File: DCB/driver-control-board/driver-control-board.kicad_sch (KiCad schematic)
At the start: 32 parts, among them J1 Conn_01x05, J2 Conn_01x14, J3 Conn_01x08, J4 Conn_01x23, J5 Conn_02x10_Counter_Clockwise, J6 Conn_01x14, U1 STM32F413CGUx, U2 LD1117S33TR_SOT223, U3 R-78B5.0-2.0, U4 MCP2551-I-SN, Y1 Crystal

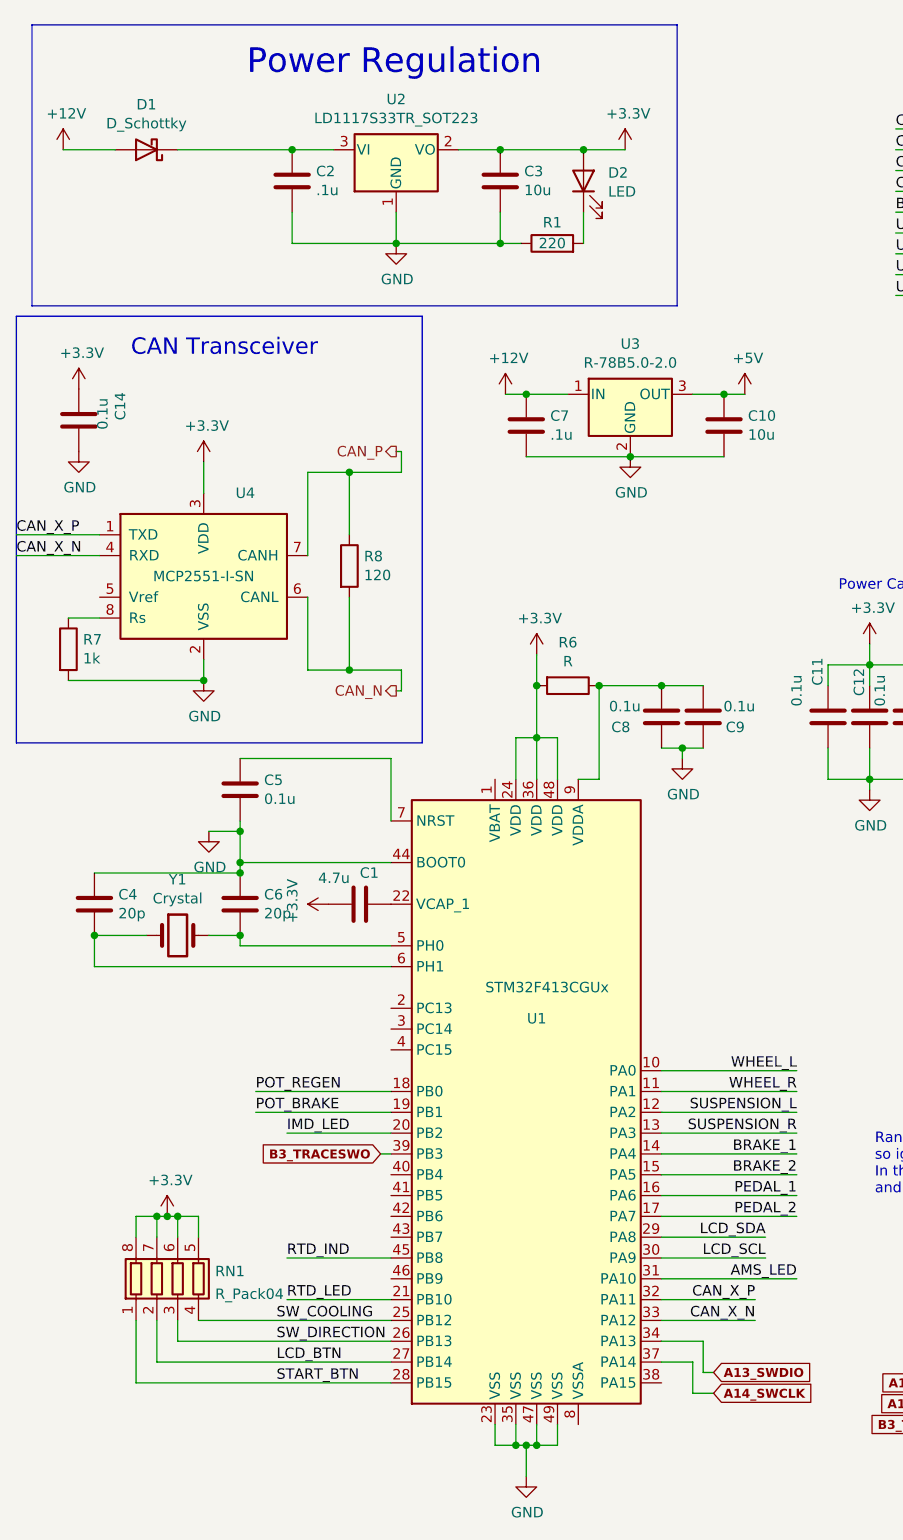
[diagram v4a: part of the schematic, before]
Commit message: Major Review and Part Update
updating footprints, component values, layouts
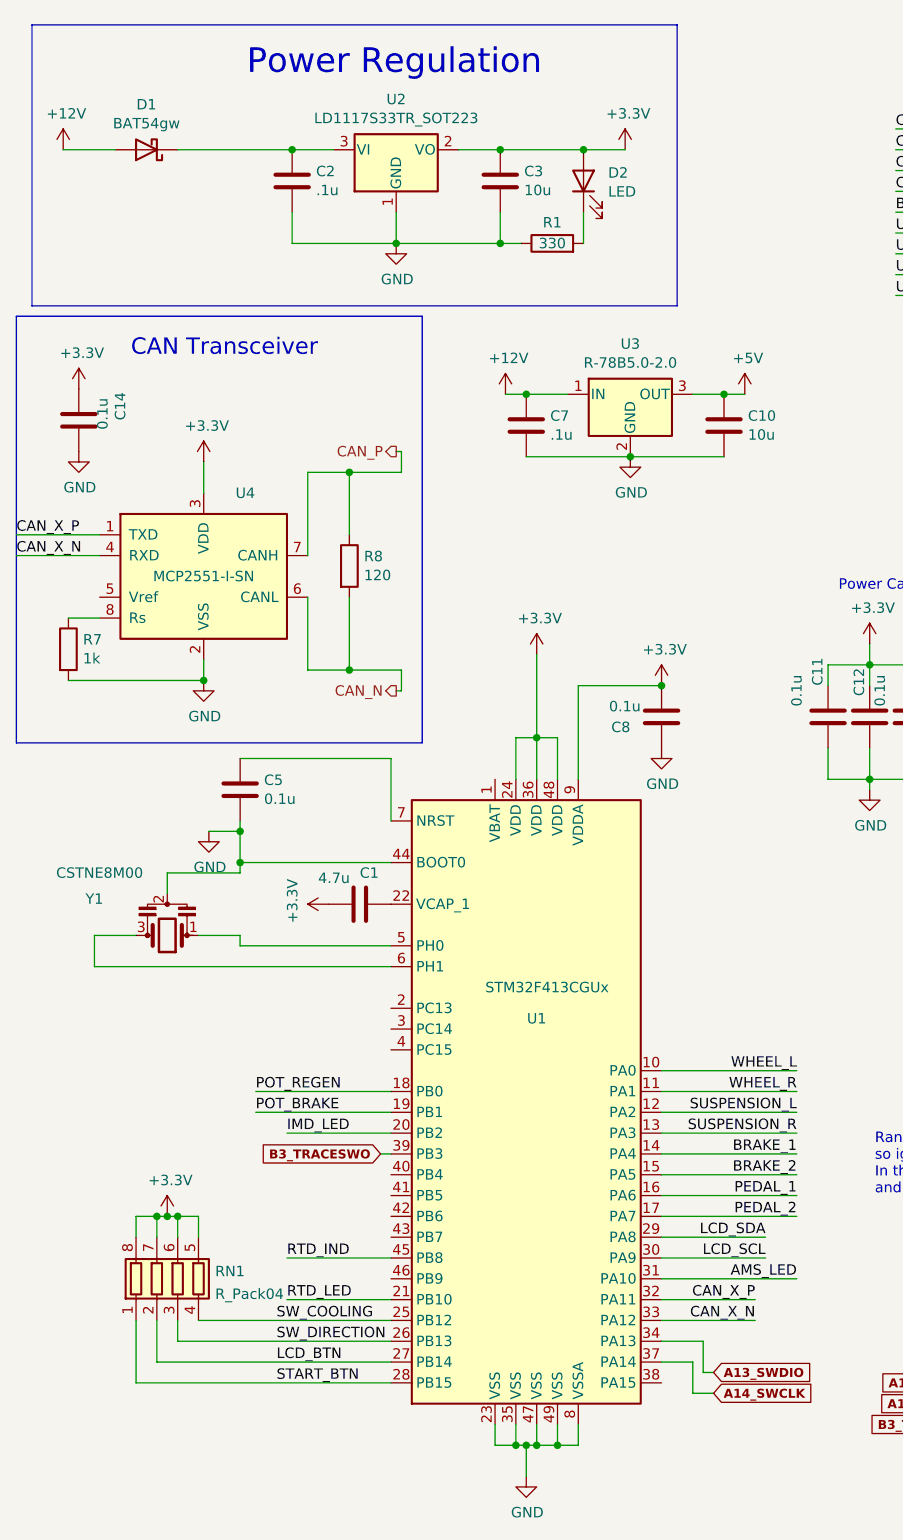
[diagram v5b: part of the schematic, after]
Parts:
- removed C4, C6: 20p, Capacitor_SMD:C_0603_1608Metric_Pad1.08x0.95mm_HandSolder, symbol Device:C
- removed C9: 0.1u, Capacitor_SMD:C_0603_1608Metric_Pad1.08x0.95mm_HandSolder, symbol Device:C
- removed R6: R, Resistor_SMD:R_0603_1608Metric_Pad0.98x0.95mm_HandSolder, symbol Device:R
- removed Y1: Crystal, Crystal:Crystal_HC52-8mm_Vertical, symbol Device:Crystal
- added Y1: CSTNE8M00, AERO_Footprints:Resonator_SMD_muRata_CSTxExxV-3Pin_3.0x1.1mm_HandSoldering, symbol Device:Resonator
- D1: value D_Schottky -> BAT54gw; footprint Diode_SMD:D_SMA-SMB_Universal_Handsoldering -> Diode_SMD:D_SOD-123
- R1: value 220 -> 330
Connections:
- net +3V3: now also C8.2, U1.9 (VDDA)
- net GND: now also U1.8 (VSSA), Y1.2
- net at U1.5 (PH0): now also Y1.1
- net at U1.6 (PH1): now also Y1.3

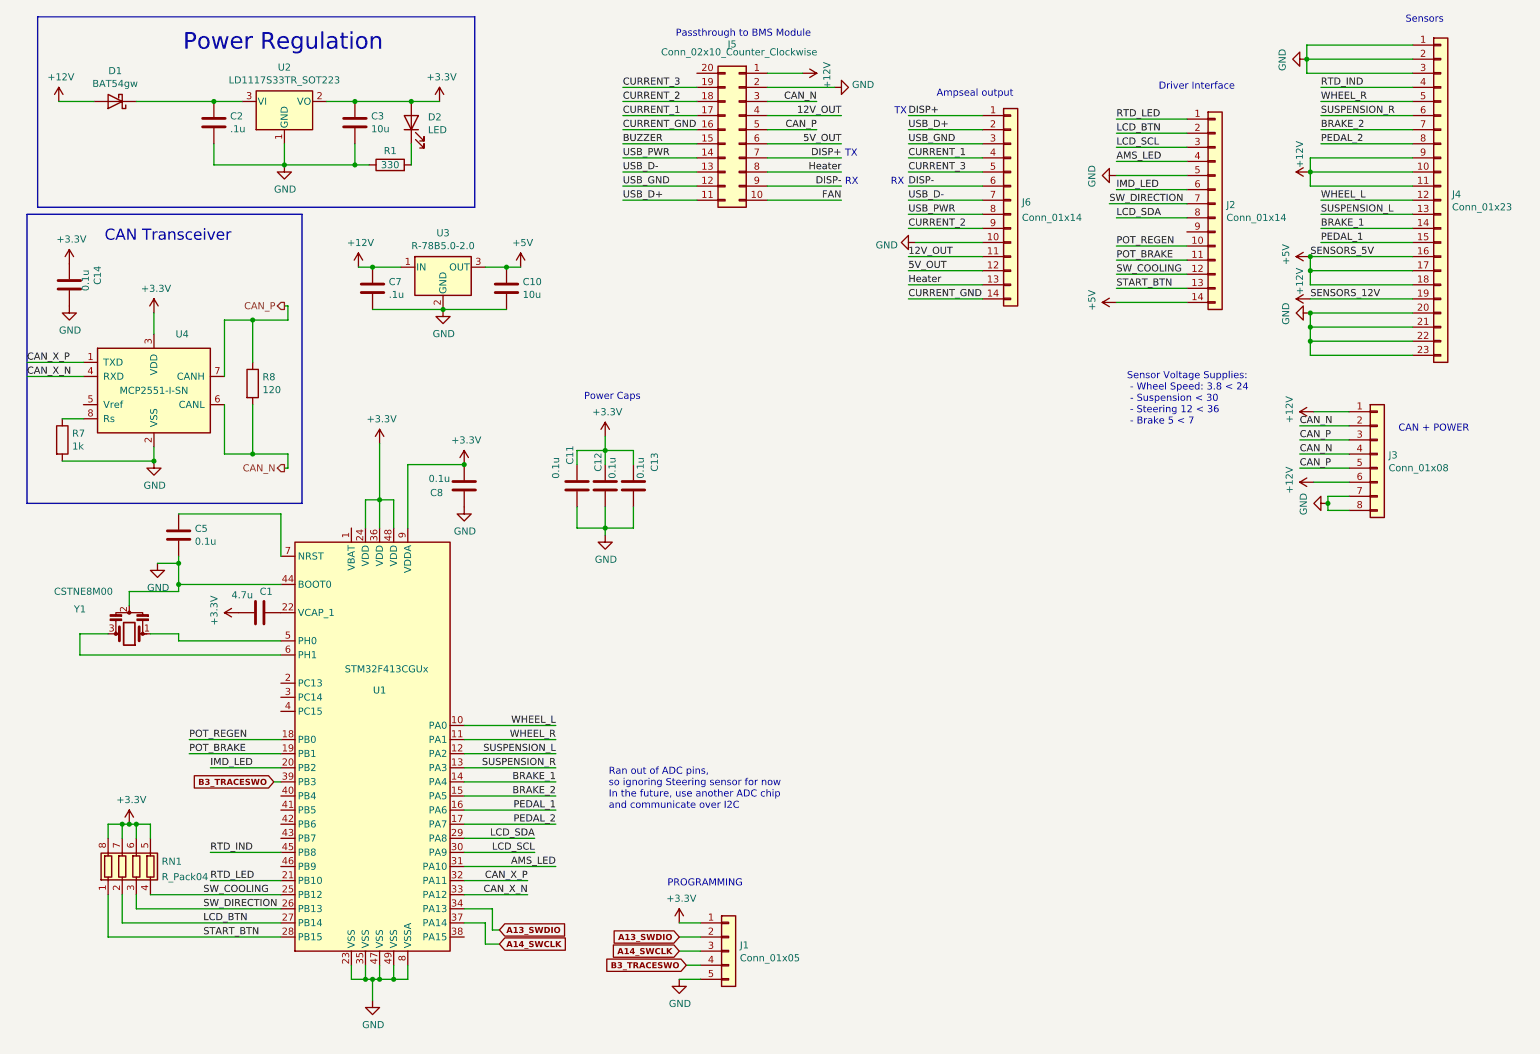
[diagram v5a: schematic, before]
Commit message: updating schematic based on RCB changes
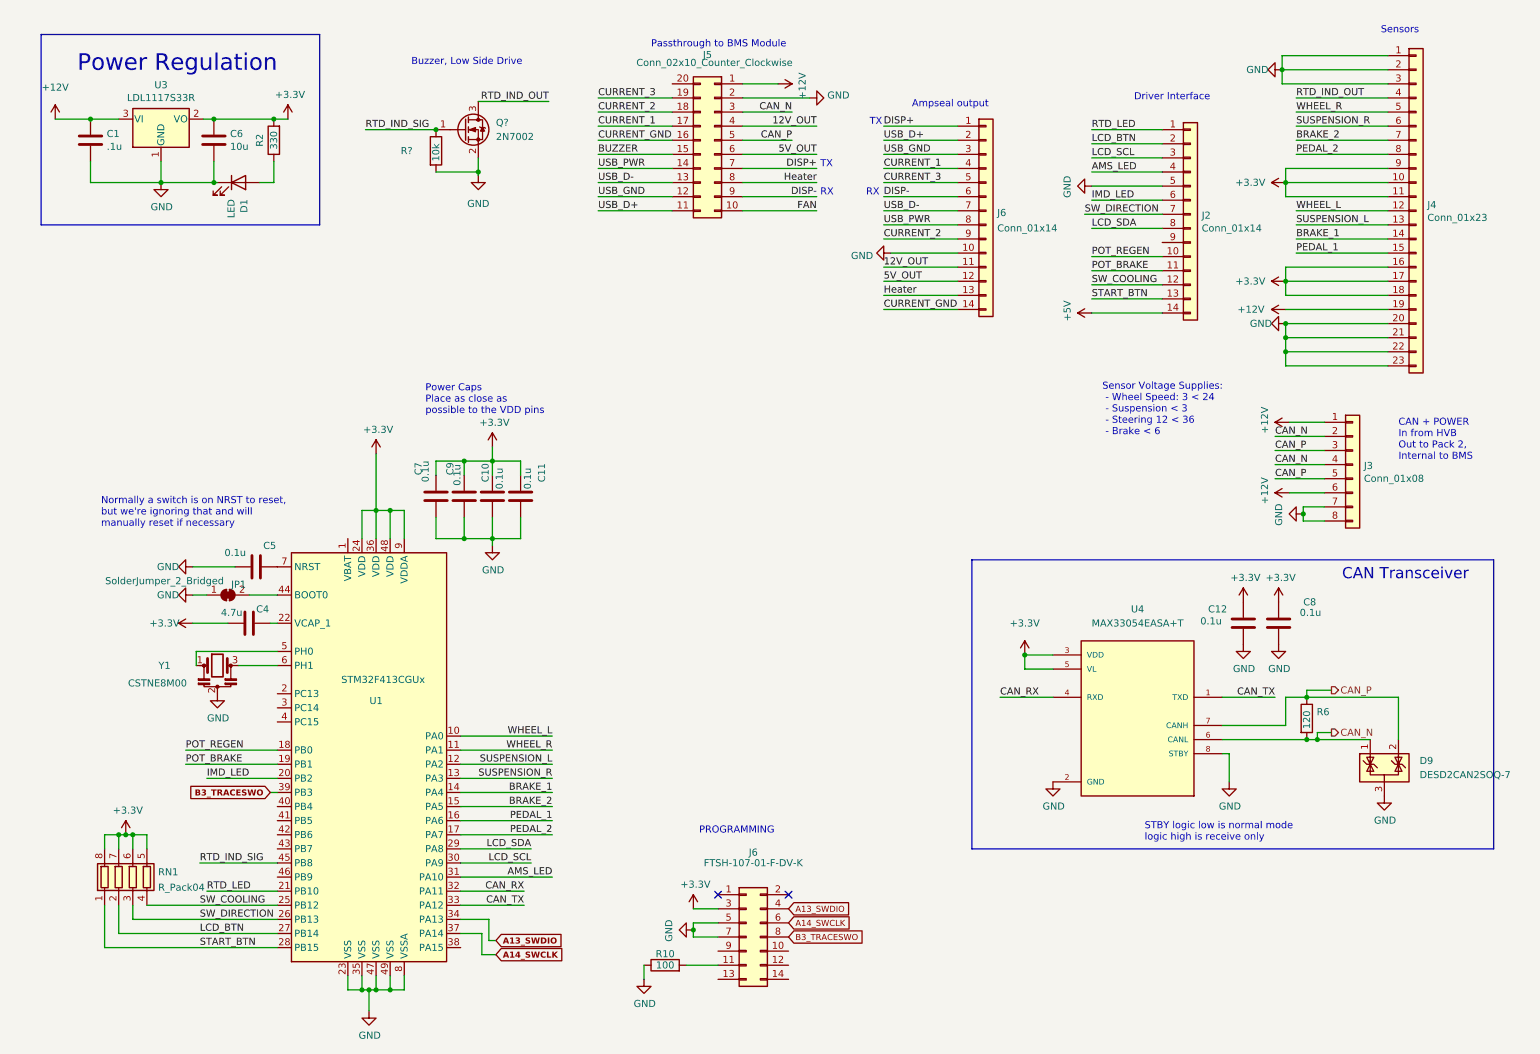
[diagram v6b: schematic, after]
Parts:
- removed C13, C14: 0.1u, Capacitor_SMD:C_0603_1608Metric_Pad1.08x0.95mm_HandSolder, symbol Device:C
- removed C2: .1u, Capacitor_SMD:C_0603_1608Metric_Pad1.08x0.95mm_HandSolder, symbol Device:C
- removed C3: 10u, Capacitor_SMD:C_0603_1608Metric_Pad1.08x0.95mm_HandSolder, symbol Device:C
- removed D1: BAT54gw, Diode_SMD:D_SOD-123, symbol Device:D_Schottky
- removed D2: LED, LED_SMD:LED_0603_1608Metric_Pad1.05x0.95mm_HandSolder, symbol Device:LED
- removed J1: Conn_01x05, Connector_JST:JST_XH_B5B-XH-A_1x05_P2.50mm_Vertical, symbol Connector_Generic:Conn_01x05
- removed R1: 330, Resistor_SMD:R_0603_1608Metric_Pad0.98x0.95mm_HandSolder, symbol Device:R
- removed R7: 1k, Resistor_SMD:R_0603_1608Metric_Pad0.98x0.95mm_HandSolder, symbol Device:R
- removed R8: 120, Resistor_SMD:R_0603_1608Metric_Pad0.98x0.95mm_HandSolder, symbol Device:R
- removed U2: LD1117S33TR_SOT223, Package_TO_SOT_SMD:SOT-223-3_TabPin2, symbol Regulator_Linear:LD1117S33TR_SOT223
- removed U3: R-78B5.0-2.0, Converter_DCDC:Converter_DCDC_RECOM_R-78B-2.0_THT, symbol Regulator_Switching:R-78B5.0-2.0
- removed U4: MCP2551-I-SN, Package_SO:SOIC-8_3.9x4.9mm_P1.27mm, symbol Interface_CAN_LIN:MCP2551-I-SN
- added C4: 4.7u, Capacitor_SMD:C_0603_1608Metric_Pad1.08x0.95mm_HandSolder, symbol Device:C
- added C6: 10u, Capacitor_SMD:C_0603_1608Metric_Pad1.08x0.95mm_HandSolder, symbol Device:C
- added C9: 0.1u, Capacitor_SMD:C_0603_1608Metric_Pad1.08x0.95mm_HandSolder, symbol Device:C
- added D1: LED, LED_SMD:LED_0603_1608Metric_Pad1.05x0.95mm_HandSolder, symbol Device:LED
- added D9: DESD2CAN2SOQ-7, Package_TO_SOT_SMD:SOT-23, symbol Power_Protection:NUP2105L
- added J6: FTSH-107-01-F-DV-K, Connector_PinHeader_1.27mm:PinHeader_2x07_P1.27mm_Vertical_SMD, symbol Connector_Generic:Conn_02x07_Odd_Even
- added JP1: SolderJumper_2_Bridged, Jumper:SolderJumper-2_P1.3mm_Bridged_Pad1.0x1.5mm, symbol Jumper:SolderJumper_2_Bridged
- added Q?: 2N7002, Package_TO_SOT_SMD:SOT-23, symbol Transistor_FET:2N7002
- added R10: 100, Resistor_SMD:R_0603_1608Metric_Pad0.98x0.95mm_HandSolder, symbol Device:R
- added R2: 330, Resistor_SMD:R_0603_1608Metric_Pad0.98x0.95mm_HandSolder, symbol Device:R
- added R6: 120, Resistor_SMD:R_0603_1608Metric_Pad0.98x0.95mm_HandSolder, symbol Device:R
- added R?: 10k, symbol Device:R
- added U3: LDL1117S33R, Package_TO_SOT_SMD:SOT-223-3_TabPin2, symbol Regulator_Linear:LD1117S33TR_SOT223
- added U4: MAX33054EASA+T, AERO_Footprints:SOIC127P600X175-8N, symbol AERO_Symbols:MAX33054EASA+T
- C1: value 4.7u -> .1u
- C10: value 10u -> 0.1u
- C7: value .1u -> 0.1u
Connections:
- net +12V: now also C1.1, U3.3 (VI); no longer C7.1, J4.10 (Pin_10), J4.11 (Pin_11), J4.9 (Pin_9)
- net +3V3: now also C10.1, C7.1, C8.1, J4.10 (Pin_10), J4.11 (Pin_11), J4.16 (Pin_16), J4.17 (Pin_17), J4.18 (Pin_18), J4.9 (Pin_9), C4.2, C6.1, C9.1, J6.3 (Pin_3), R2.2, U3.2 (VO), U4.3 (VDD), U4.5 (VL); no longer C1.2, C8.2
- net +5V: no longer C10.1, J4.16 (Pin_16), J4.17 (Pin_17), J4.18 (Pin_18)
- net A13_SWDIO: now also J6.4 (Pin_4)
- net A14_SWCLK: now also J6.6 (Pin_6)
- net B3_TRACESWO: now also J6.8 (Pin_8)
- net CAN_N: now also D9.1 (K), R6.2, U4.6 (CANL)
- net CAN_P: now also D9.2 (K), R6.1, U4.7 (CANH)
- net GND: now also C1.2, C8.2, C6.2, C9.2, D1.1 (K), D9.3 (A), J6.5 (Pin_5), J6.7 (Pin_7), JP1.1 (A), Q?.2 (S), R10.1, R?.2, U3.1 (GND), U4.2 (GND), U4.8 (STBY); no longer C8.1, U1.44 (BOOT0)
- net at U1.22 (VCAP_1): now also C4.1; no longer C1.1
- net CAN_X_N renamed CAN_TX
- net CAN_TX: now also U4.1 (TXD)
- net CAN_X_P renamed CAN_RX
- net CAN_RX: now also U4.4 (RXD)
- net RTD_IND renamed RTD_IND_OUT
- net RTD_IND_OUT: now also Q?.3 (D); no longer U1.45 (PB8)
- new net: J6.11 (Pin_11), R10.2
- new net: JP1.2 (B), U1.44 (BOOT0)
- new net: D1.2 (A), R2.1
- new net RTD_IND_SIG: Q?.1 (G), R?.1, U1.45 (PB8)
- no-connect marks 0 -> 2
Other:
- note added: "Buzzer, Low Side Drive"
- note added: "CAN + POWER In from HVB Out to Pack 2, Internal to BMS"
- note added: "Normally a switch is on NRST to reset, but we're ignoring that and will manually reset if necessary"
- note added: "Power Caps Place as close as possible to the VDD pins"
- note added: "STBY logic low is normal mode logic high is receive only"
- note added: "Sensor Voltage Supplies: - Wheel Speed: 3 < 24 - Suspension < 3 - Steering 12 < 36 - Brake < 6"
- note removed: "CAN + POWER"
- note removed: "Power Caps"
- note removed: "Ran out of ADC pins, so ignoring Steering sensor for now In the future, use another ADC chip and communicate over I2C"
- note removed: "Sensor Voltage Supplies: - Wheel Speed: 3.8 < 24 - Suspension < 30 - Steering 12 < 36 - Brake 5 < 7"
- moved on the sheet: J2, J3, J4, J5, J6, RN1

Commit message: updating schem and layout. WIP
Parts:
- added D2, D3, D4, D5, D6: SP0502BAHT, Package_TO_SOT_SMD:SOT-23, symbol Power_Protection:SP0502BAHT
- R1: renamed from R?; footprint (none) -> Resistor_SMD:R_0603_1608Metric_Pad0.98x0.95mm_HandSolder
- gave numbers to parts that had none: 1
- renumbered J6 to J7
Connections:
- net BRAKE_1: now also D4.2 (K)
- net BRAKE_2: now also D4.1 (K)
- net GND: now also D2.3 (A), D3.3 (A), D4.3 (A), D5.3 (A), D6.3 (A)
- net PEDAL_1: now also D3.2 (K)
- net PEDAL_2: now also D3.1 (K)
- net POT_BRAKE: now also D2.2 (K)
- net POT_REGEN: now also D2.1 (K)
- net SUSPENSION_L: now also D5.2 (K)
- net SUSPENSION_R: now also D5.1 (K)
- net WHEEL_L: now also D6.2 (K)
- net WHEEL_R: now also D6.1 (K)
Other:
- moved on the sheet: J7, R10

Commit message: finished schem and layout. Ready for Review
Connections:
- net +5V is gone; now on net +3V3: J2.14 (Pin_14)
- net +12V: now also J4.16 (Pin_16); no longer J4.19 (Pin_19)
- net +3V3: no longer J4.16 (Pin_16)
- net GND: no longer J4.1 (Pin_1)
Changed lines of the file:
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@@
-    (stroke (width 0) (type default) (color 0 0 0 0))
-  )
-  (wire (pts (xy 242.57 59.055) (xy 242.57 61.595))
     (stroke (width 0) (type default) (color 0 0 0 0))
   )
@@
   )
   (wire (pts (xy 158.115 43.815) (xy 144.78 43.815))
-    (stroke (width 0) (type default) (color 0 0 0 0))
-  )
-  (wire (pts (xy 241.935 23.495) (xy 241.935 20.955))
     (stroke (width 0) (type default) (color 0 0 0 0))
   )
@@
     (pin "1")
   )
-  (symbol (lib_id "power:+5V") (at 207.645 67.31 90) (unit 1)
-    (in_bom yes) (on_board yes)
-    (property "Reference" "#PWR0115" (id 0) (at 211.455 67.31 0)
-      (effects (font (size 1.27 1.27)) hide)
-    )
-    (property "Value" "+5V" (id 1) (at 203.2508 66.929 0))
-    (property "Footprint" "" (id 2) (at 207.645 67.31 0)
-      (effects (font (size 1.27 1.27)) hide)
-    )
-    (property "Datasheet" "" (id 3) (at 207.645 67.31 0)
-      (effects (font (size 1.27 1.27)) hide)
-    )
-    (pin "1")
-  )
   (symbol (lib_id "power:GND") (at 207.645 44.45 270) (unit 1)
     (in_bom yes) (on_board yes)
@@
     (pin "8")
   )
-  (symbol (lib_id "power:+12V") (at 242.57 66.675 90) (unit 1)
+  (symbol (lib_id "power:+12V") (at 242.57 59.055 90) (unit 1)
     (in_bom yes) (on_board yes) (fields_autoplaced)
-    (property "Reference" "#PWR0101" (id 0) (at 246.38 66.675 0)
-      (effects (font (size 1.27 1.27)) hide)
-    )
-    (property "Value" "+12V" (id 1) (at 238.76 66.6749 90)
-      (effects (font (size 1.27 1.27)) (justify left))
-    )
-    (property "Footprint" "" (id 2) (at 242.57 66.675 0)
-      (effects (font (size 1.27 1.27)) hide)
-    )
-    (property "Datasheet" "" (id 3) (at 242.57 66.675 0)
+    (property "Reference" "#PWR0101" (id 0) (at 246.38 59.055 0)
+      (effects (font (size 1.27 1.27)) hide)
+    )
+    (property "Value" "+12V" (id 1) (at 238.76 59.0549 90)
+      (effects (font (size 1.27 1.27)) (justify left))
+    )
+    (property "Footprint" "" (id 2) (at 242.57 59.055 0)
+      (effects (font (size 1.27 1.27)) hide)
+    )
+    (property "Datasheet" "" (id 3) (at 242.57 59.055 0)
       (effects (font (size 1.27 1.27)) hide)
     )
@@
     (pin "3")
   )
+  (symbol (lib_id "power:+3.3V") (at 207.645 67.31 90) (unit 1)
+    (in_bom yes) (on_board yes)
+    (property "Reference" "#PWR0115" (id 0) (at 211.455 67.31 0)
+      (effects (font (size 1.27 1.27)) hide)
+    )
+    (property "Value" "+3.3V" (id 1) (at 201.295 67.31 90))
+    (property "Footprint" "" (id 2) (at 207.645 67.31 0)
+      (effects (font (size 1.27 1.27)) hide)
+    )
+    (property "Datasheet" "" (id 3) (at 207.645 67.31 0)
+      (effects (font (size 1.27 1.27)) hide)
+    )
+    (pin "1")
+  )
   (symbol (lib_id "power:GND") (at 241.935 23.495 270) (unit 1)
     (in_bom yes) (on_board yes)
@@
       (reference "#PWR0114") (unit 1) (value "+3.3V") (footprint "")
     )
-    (path "/00000000-0000-0000-0000-000061fdabd7"
-      (reference "#PWR0115") (unit 1) (value "+5V") (footprint "")
+    (path "/f7db3756-bfcc-4fbd-af9e-ae41e26d5446"
+      (reference "#PWR0115") (unit 1) (value "+3.3V") (footprint "")
     )
     (path "/19dd25e8-ec01-467b-bde1-31fa668445ca"
